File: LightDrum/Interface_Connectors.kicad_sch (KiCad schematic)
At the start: 3 parts, among them J2 0525593652, J3 0541323662, J4 PWR-CONN

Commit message: PCB Lock REV11
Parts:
- removed J3: 0541323662, Daxxn_Connectors:0541323662, symbol Daxxn_Connectors:0541323662
- added J0: 0541323662, Daxxn_Connectors:0541323662, symbol Daxxn_Connectors:0541323662
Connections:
- net Vdrive is gone; now on net VDD: J2.1 (Pin_1)
- net AUDIO-SRC-IND: now also J2.34 (Pin_34), J0.34 (Pin_34); no longer J2.3 (Pin_3)
- net DIAG-DEBUG_{PWM}: now also J2.33 (Pin_33); no longer J2.4 (Pin_4)
- net DIAG-STATUS_{PWM}: now also J2.32 (Pin_32); no longer J2.5 (Pin_5)
- net ENC1-A: now also J2.16 (Pin_16), J0.16 (Pin_16); no longer J2.21 (Pin_21)
- net ENC1-B: now also J2.23 (Pin_23), J0.23 (Pin_23); no longer J2.14 (Pin_14)
- net ENC1-SW: now also J2.10 (Pin_10), J0.10 (Pin_10); no longer J2.27 (Pin_27)
- net ENC2-A: now also J2.14 (Pin_14), J0.14 (Pin_14); no longer J2.23 (Pin_23)
- net ENC2-B: now also J2.12 (Pin_12), J0.12 (Pin_12); no longer J2.25 (Pin_25)
- net ENC2-SW: now also J2.18 (Pin_18), J0.18 (Pin_18); no longer J2.19 (Pin_19)
- net GND: now also J2.5 (Pin_5), J0.5 (Pin_5), J0.M (MNT); no longer J2.32 (Pin_32)
- net GRAPH-CLK_{S}: now also J2.6 (Pin_6); no longer J2.31 (Pin_31)
- net GRAPH-LE_{S}: now also J2.25 (Pin_25); no longer J2.12 (Pin_12)
- net GRAPH-SDI_{S}: now also J2.24 (Pin_24); no longer J2.13 (Pin_13)
- net GRAPH-~{OE}_{S}: now also J2.27 (Pin_27); no longer J2.10 (Pin_10)
- net I2C-SCLK_{S}: now also J2.15 (Pin_15); no longer J2.22 (Pin_22)
- net I2C-SDA_{S}: now also J2.13 (Pin_13); no longer J2.24 (Pin_24)
- net MENU-ACT: now also J0.20 (Pin_20)
- net MENU-ACT_{INT}: now also J2.20 (Pin_20); no longer J2.17 (Pin_17)
- net MENU-BACK: now also J0.21 (Pin_21)
- net MENU-BACK_{INT}: now also J2.21 (Pin_21); no longer J2.16 (Pin_16)
- net MENU-DOWN: now also J0.26 (Pin_26)
- net MENU-DOWN_{INT}: now also J2.26 (Pin_26); no longer J2.11 (Pin_11)
- net MENU-LEFT: now also J0.8 (Pin_8)
- net MENU-LEFT_{INT}: now also J2.8 (Pin_8); no longer J2.29 (Pin_29)
- net MENU-RIGHT: now also J0.19 (Pin_19)
- net MENU-RIGHT_{INT}: now also J2.19 (Pin_19); no longer J2.18 (Pin_18)
- net MENU-UP: now also J0.22 (Pin_22)
- net MENU-UP_{INT}: now also J2.22 (Pin_22); no longer J2.15 (Pin_15)
- net MIDI-IN_{S}: now also J2.3 (Pin_3); no longer J2.34 (Pin_34)
- net MIDI-OUT_{S}: now also J2.2 (Pin_2); no longer J2.35 (Pin_35)
- net SCR-RX_{S}: now also J2.9 (Pin_9); no longer J2.28 (Pin_28)
- net SCR-TX_{S}: now also J2.7 (Pin_7); no longer J2.30 (Pin_30)
- net SD-CD_{S}: now also J2.17 (Pin_17); no longer J2.20 (Pin_20)
- net SD-CLK_{S}: now also J2.28 (Pin_28); no longer J2.9 (Pin_9)
- net SD-CMD_{S}: now also J2.30 (Pin_30); no longer J2.7 (Pin_7)
- net SD-D0_{S}: now also J2.29 (Pin_29); no longer J2.8 (Pin_8)
- net STRIP-PWR: now also J2.31 (Pin_31), J0.31 (Pin_31); no longer J2.6 (Pin_6)
- net VCC: now also J2.11 (Pin_11), J0.11 (Pin_11); no longer J2.26 (Pin_26)
- net VDD: now also J2.35 (Pin_35), J0.1 (Pin_1), J0.35 (Pin_35); no longer J2.2 (Pin_2), J2.36 (Pin_36)
- net ~{RESET}_{C}: now also J2.4 (Pin_4); no longer J2.33 (Pin_33)
- new net DIAG-DEBUG: J0.33 (Pin_33)
- new net DIAG-STATUS: J0.32 (Pin_32)
- new net GRAPH-CLK: J0.6 (Pin_6)
- new net GRAPH-LE: J0.25 (Pin_25)
- new net GRAPH-SDI: J0.24 (Pin_24)
- new net GRAPH-~{OE}: J0.27 (Pin_27)
- new net I2C-SCLK: J0.15 (Pin_15)
- new net I2C-SDA: J0.13 (Pin_13)
- new net MIDI-IN: J0.3 (Pin_3)
- new net MIDI-OUT: J0.2 (Pin_2)
- new net SCR-RX: J0.9 (Pin_9)
- new net SCR-TX: J0.7 (Pin_7)
- new net SD-CD: J0.17 (Pin_17)
- new net SD-CLK: J0.28 (Pin_28)
- new net SD-CMD: J0.30 (Pin_30)
- new net SD-D0: J0.29 (Pin_29)
- new net STRIP-PG: J0.36 (Pin_36), J2.36 (Pin_36)
- new net ~{RESET}: J0.4 (Pin_4)
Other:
- note added: "MATCHING CONN ON INTERFACE PCB -NOT POPULATED-"
- note removed: "MATCHING CONN ON INTERFACE PCB NOT POPULATED"
- moved on the sheet: J2

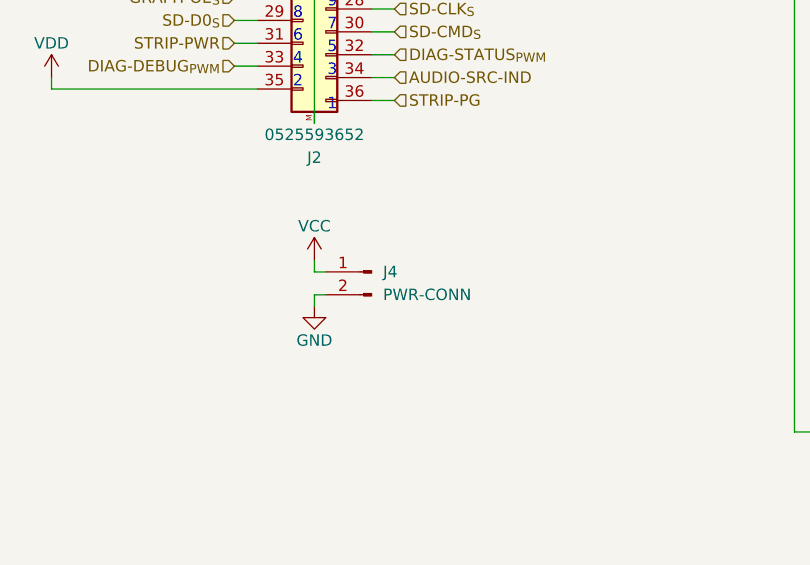
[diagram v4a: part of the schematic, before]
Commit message: Replace DSub with much better ECU conn
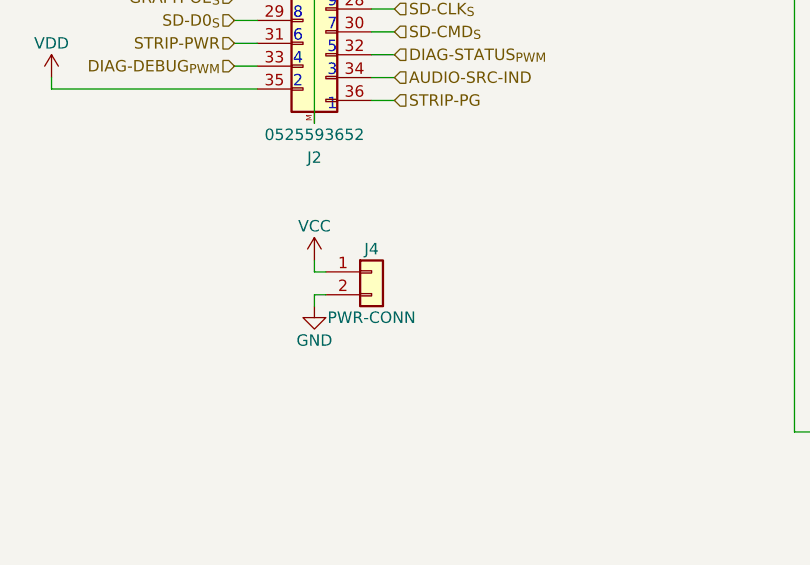
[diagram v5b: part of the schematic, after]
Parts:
- removed J4: PWR-CONN, Daxxn_Connectors:JST_XH_B2B-XH-A_Vertical, symbol Connector:Conn_01x02_Male
- added J4: PWR-CONN, Daxxn_Connectors:JST_XH_B2B-XH-A_Vertical, symbol Connector_Generic:Conn_01x02
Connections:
- net GND: now also J4.2 (Pin_2)
- net VCC: now also J4.1 (Pin_1)
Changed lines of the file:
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@@
-    )
-  )
-  (symbol (lib_id "Connector:Conn_01x02_Male") (at 57.15 110.49 0) (mirror y) (unit 1)
-    (in_bom yes) (on_board yes) (dnp no)
-    (property "Reference" "J4" (at 58.42 110.49 0)
-      (effects (font (size 1.27 1.27)) (justify right))
-    )
-    (property "Value" "PWR-CONN" (at 58.42 113.03 0)
-      (effects (font (size 1.27 1.27)) (justify right))
-    )
-    (property "Footprint" "Daxxn_Connectors:JST_XH_B2B-XH-A_Vertical" (at 57.15 110.49 0)
-      (effects (font (size 1.27 1.27)) hide)
-    )
-    (property "Datasheet" "~" (at 57.15 110.49 0)
-      (effects (font (size 1.27 1.27)) hide)
-    )
-    (property "SupplierPN" "455-2247-ND" (at 57.15 110.49 0)
-      (effects (font (size 1.27 1.27)) hide)
-    )
-    (pin "1")
-    (pin "2")
-    (instances
-      (project "LightDrum"
-        (path "/7f137461-fd46-4a4c-8db7-555d487fb3ca/37b1a4e5-7bc5-4d58-948d-cb24160396b1"
-          (reference "J4") (unit 1)
-        )
-      )
     )
   )
@@
         )
       )
+    )
+  )
+  (symbol (lib_id "Connector_Generic:Conn_01x02") (at 57.15 110.49 0) (unit 1)
+    (in_bom yes) (on_board yes) (dnp no)
+    (property "Reference" "J4" (at 57.15 107.95 0)
+      (effects (font (size 1.27 1.27)))
+    )
+    (property "Value" "PWR-CONN" (at 57.15 115.57 0)
+      (effects (font (size 1.27 1.27)))
+    )
+    (property "Footprint" "Daxxn_Connectors:JST_XH_B2B-XH-A_Vertical" (at 57.15 110.49 0)
+      (effects (font (size 1.27 1.27)) hide)
+    )
+    (property "Datasheet" "~" (at 57.15 110.49 0)
+      (effects (font (size 1.27 1.27)) hide)
+    )
+    (property "Schematic" "" (at 57.15 110.49 0)
+      (effects (font (size 1.27 1.27)) hide)
+    )
+    (property "PartNumber" "" (at 57.15 110.49 0)
+      (effects (font (size 1.27 1.27)))
+    )
+    (property "SupplierPN" "455-2247-ND" (at 57.15 110.49 0)
+      (effects (font (size 1.27 1.27)) hide)
+    )
+    (pin "1")
+    (pin "2")
+    (instances
+      (project "LightDrum"
+        (path "/7f137461-fd46-4a4c-8db7-555d487fb3ca/37b1a4e5-7bc5-4d58-948d-cb24160396b1"
+          (reference "J4") (unit 1)
+        )
+      )

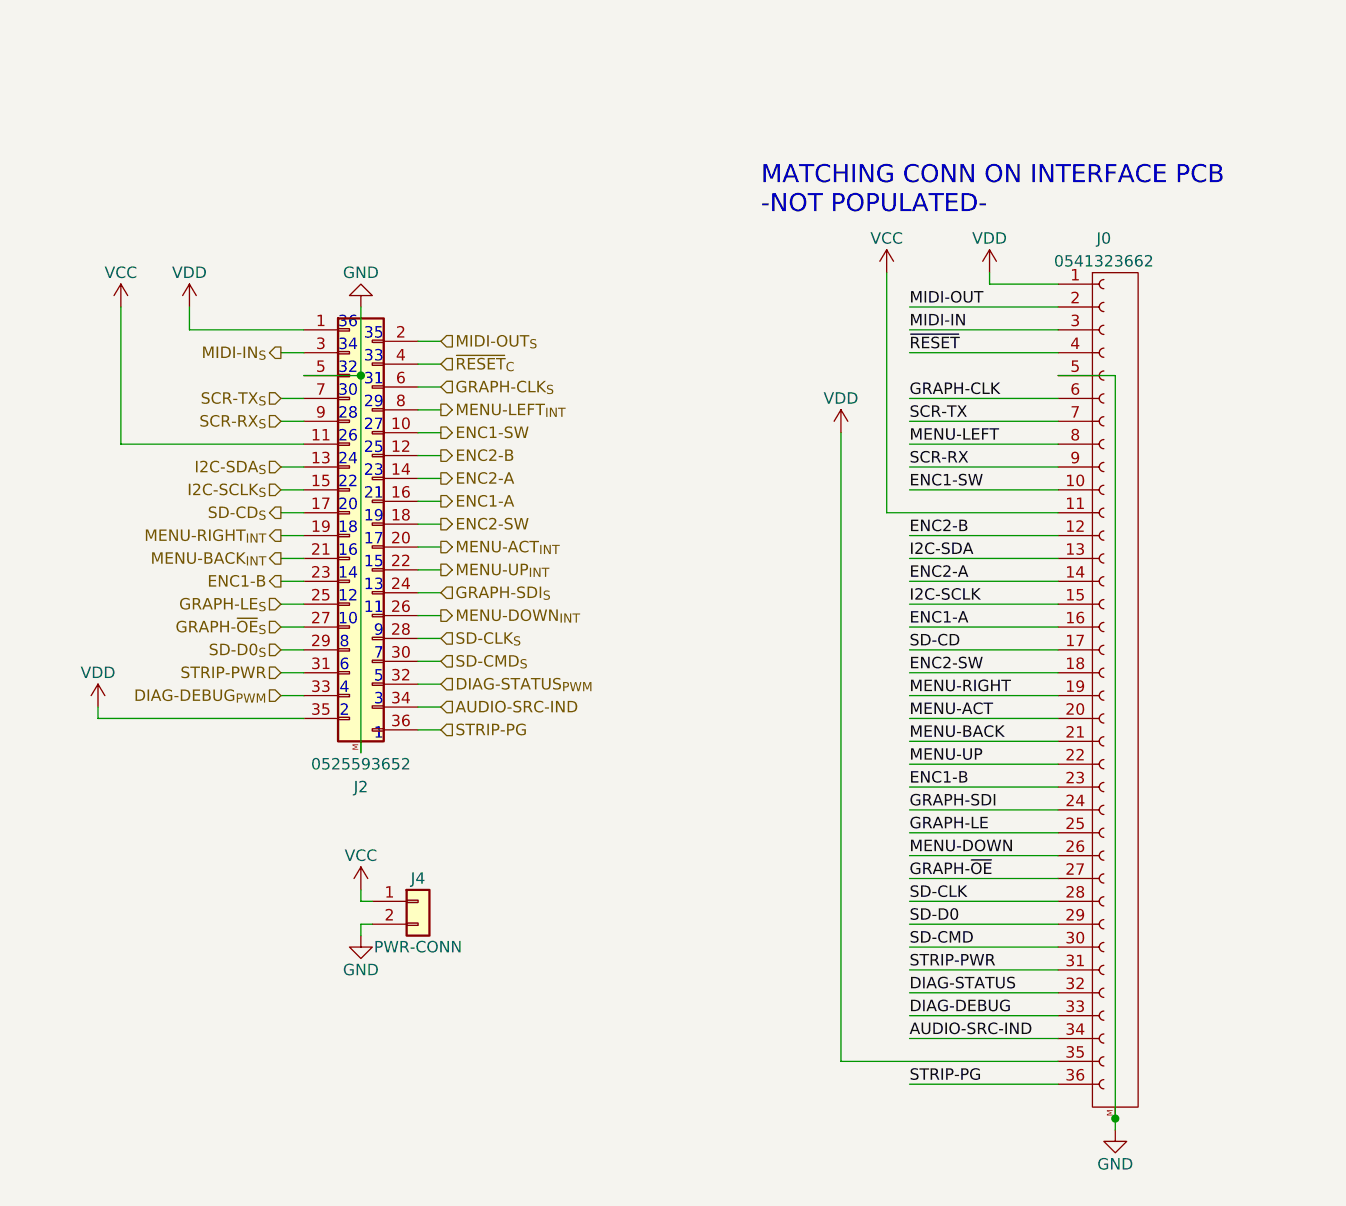
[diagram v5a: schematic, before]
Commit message: Organize old files and generate interface gerbers
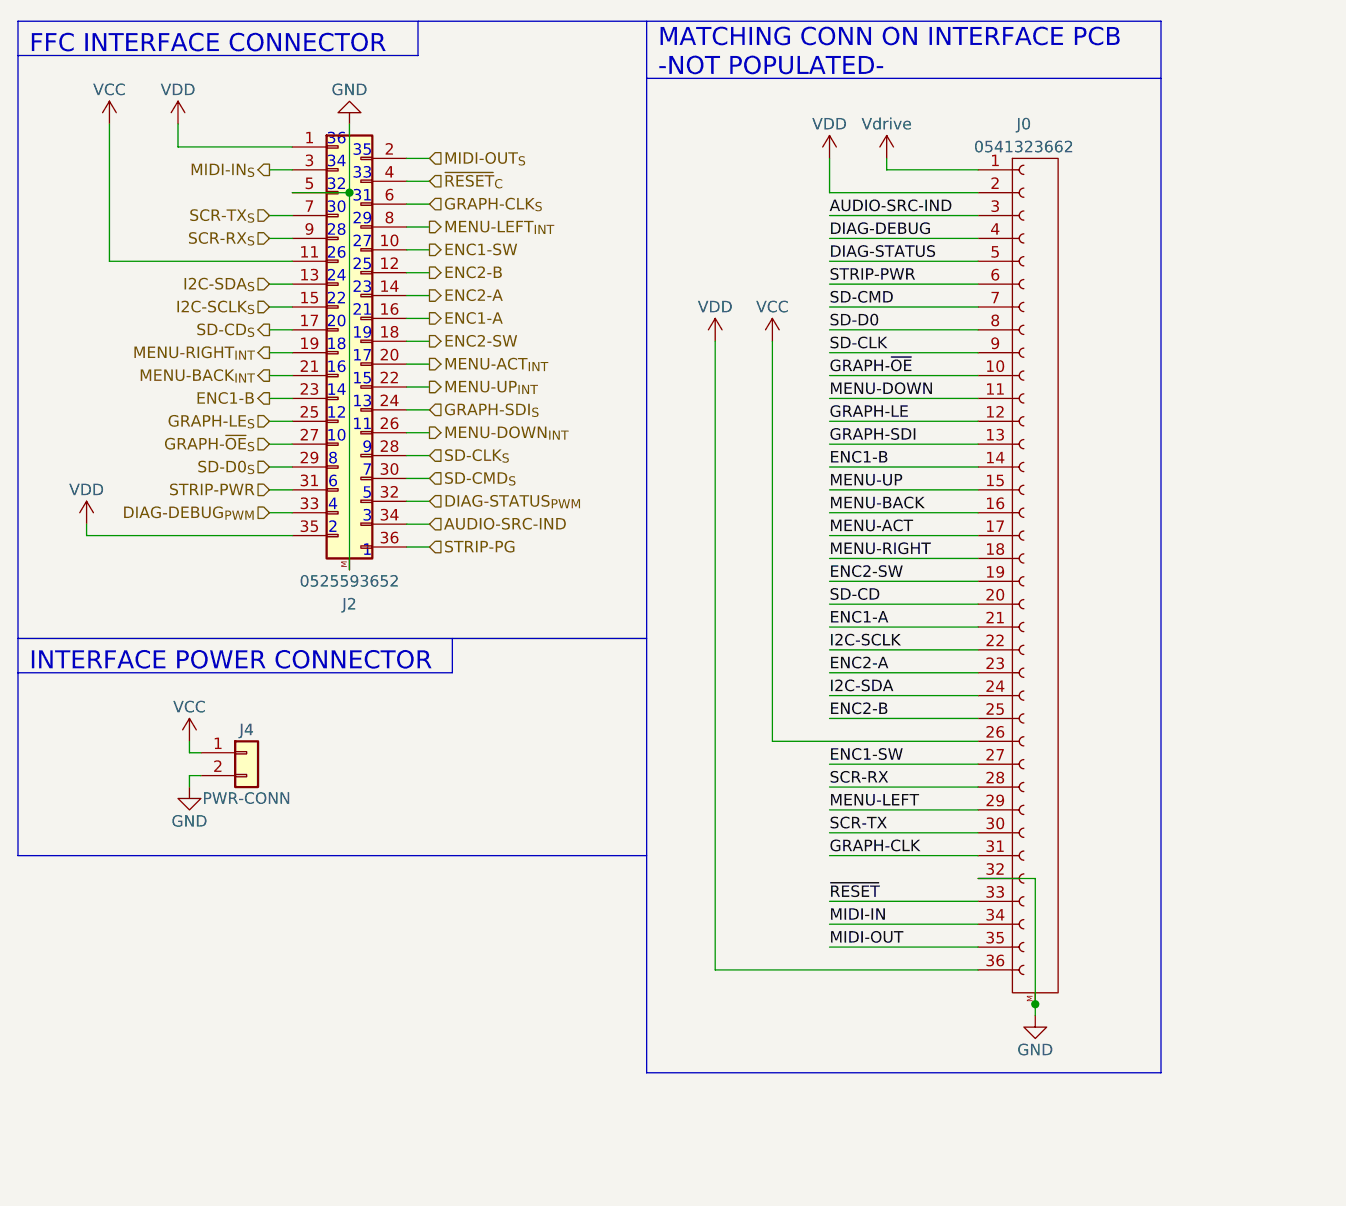
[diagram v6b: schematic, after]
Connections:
- net AUDIO-SRC-IND: now also J0.3 (Pin_3); no longer J0.34 (Pin_34)
- net DIAG-DEBUG: now also J0.4 (Pin_4); no longer J0.33 (Pin_33)
- net DIAG-STATUS: now also J0.5 (Pin_5); no longer J0.32 (Pin_32)
- net ENC1-A: now also J0.21 (Pin_21); no longer J0.16 (Pin_16)
- net ENC1-B: now also J0.14 (Pin_14); no longer J0.23 (Pin_23)
- net ENC1-SW: now also J0.27 (Pin_27); no longer J0.10 (Pin_10)
- net ENC2-A: now also J0.23 (Pin_23); no longer J0.14 (Pin_14)
- net ENC2-B: now also J0.25 (Pin_25); no longer J0.12 (Pin_12)
- net ENC2-SW: now also J0.19 (Pin_19); no longer J0.18 (Pin_18)
- net GND: now also J0.32 (Pin_32); no longer J0.5 (Pin_5)
- net GRAPH-CLK: now also J0.31 (Pin_31); no longer J0.6 (Pin_6)
- net GRAPH-LE: now also J0.12 (Pin_12); no longer J0.25 (Pin_25)
- net GRAPH-SDI: now also J0.13 (Pin_13); no longer J0.24 (Pin_24)
- net GRAPH-~{OE}: now also J0.10 (Pin_10); no longer J0.27 (Pin_27)
- net I2C-SCLK: now also J0.22 (Pin_22); no longer J0.15 (Pin_15)
- net I2C-SDA: now also J0.24 (Pin_24); no longer J0.13 (Pin_13)
- net MENU-ACT: now also J0.17 (Pin_17); no longer J0.20 (Pin_20)
- net MENU-BACK: now also J0.16 (Pin_16); no longer J0.21 (Pin_21)
- net MENU-DOWN: now also J0.11 (Pin_11); no longer J0.26 (Pin_26)
- net MENU-LEFT: now also J0.29 (Pin_29); no longer J0.8 (Pin_8)
- net MENU-RIGHT: now also J0.18 (Pin_18); no longer J0.19 (Pin_19)
- net MENU-UP: now also J0.15 (Pin_15); no longer J0.22 (Pin_22)
- net MIDI-IN: now also J0.34 (Pin_34); no longer J0.3 (Pin_3)
- net MIDI-OUT: now also J0.35 (Pin_35); no longer J0.2 (Pin_2)
- net SCR-RX: now also J0.28 (Pin_28); no longer J0.9 (Pin_9)
- net SCR-TX: now also J0.30 (Pin_30); no longer J0.7 (Pin_7)
- net SD-CD: now also J0.20 (Pin_20); no longer J0.17 (Pin_17)
- net SD-CLK: now also J0.9 (Pin_9); no longer J0.28 (Pin_28)
- net SD-CMD: now also J0.7 (Pin_7); no longer J0.30 (Pin_30)
- net SD-D0: now also J0.8 (Pin_8); no longer J0.29 (Pin_29)
- net STRIP-PG: no longer J0.36 (Pin_36)
- net STRIP-PWR: now also J0.6 (Pin_6); no longer J0.31 (Pin_31)
- net VCC: now also J0.26 (Pin_26); no longer J0.11 (Pin_11)
- net VDD: now also J0.2 (Pin_2), J0.36 (Pin_36); no longer J0.1 (Pin_1), J0.35 (Pin_35)
- net ~{RESET}: now also J0.33 (Pin_33); no longer J0.4 (Pin_4)
- new net Vdrive: J0.1 (Pin_1)
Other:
- note added: "FFC INTERFACE CONNECTOR"
- note added: "INTERFACE POWER CONNECTOR"
- moved on the sheet: J2, J4
